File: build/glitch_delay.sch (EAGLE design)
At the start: 55 parts

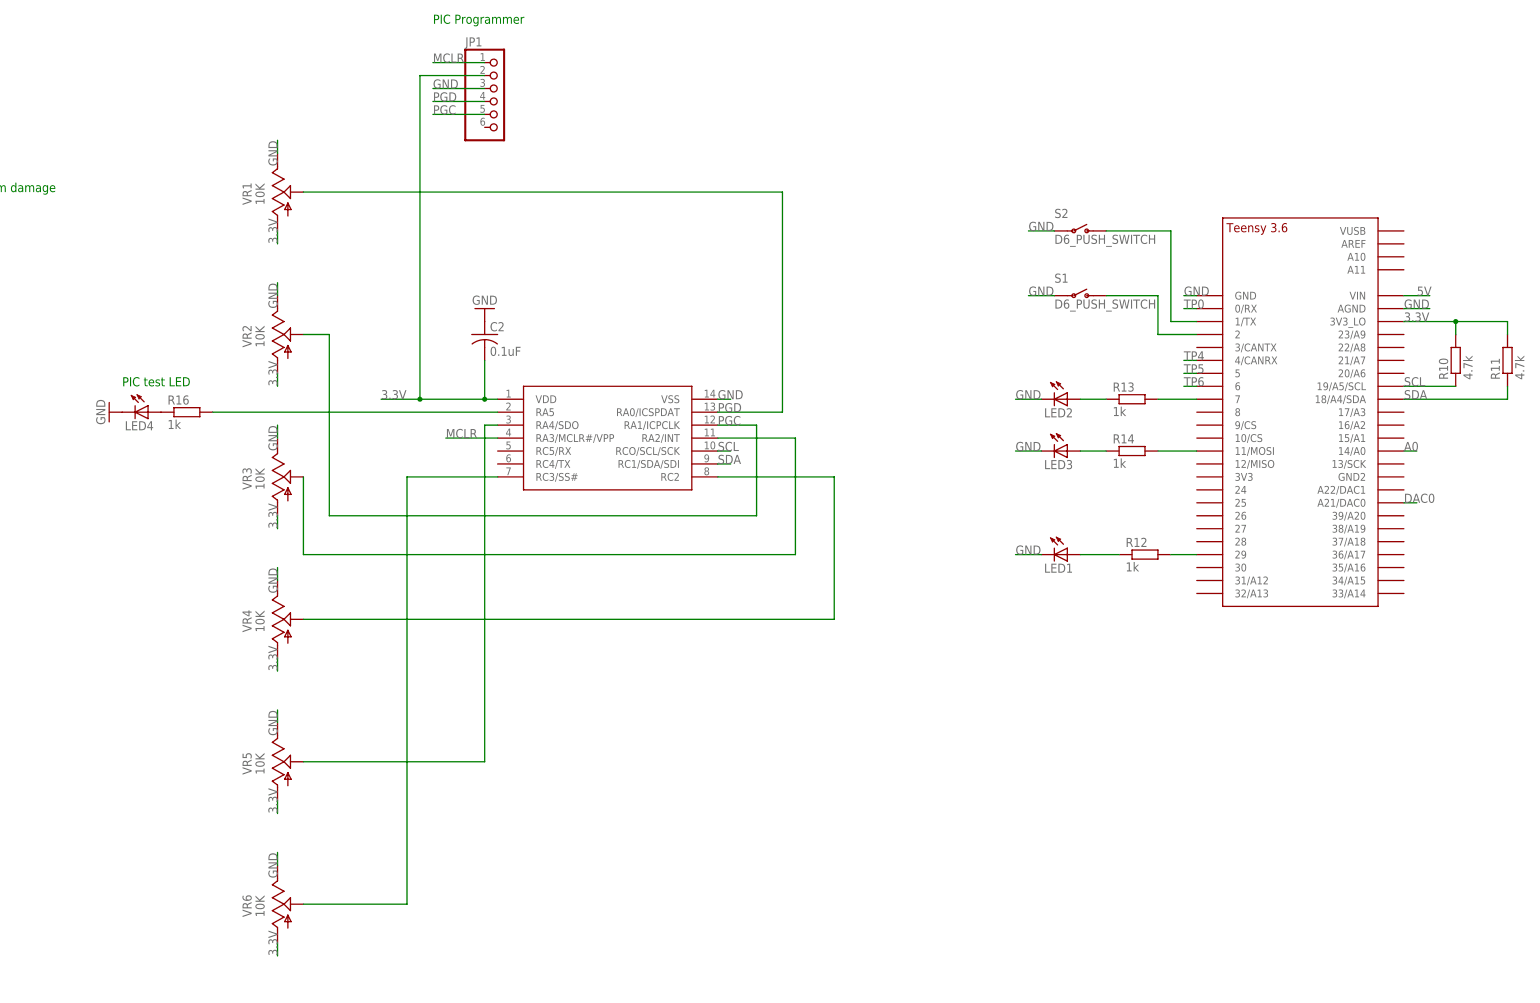
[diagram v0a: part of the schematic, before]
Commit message: Removing PIC from board and using ADC1.
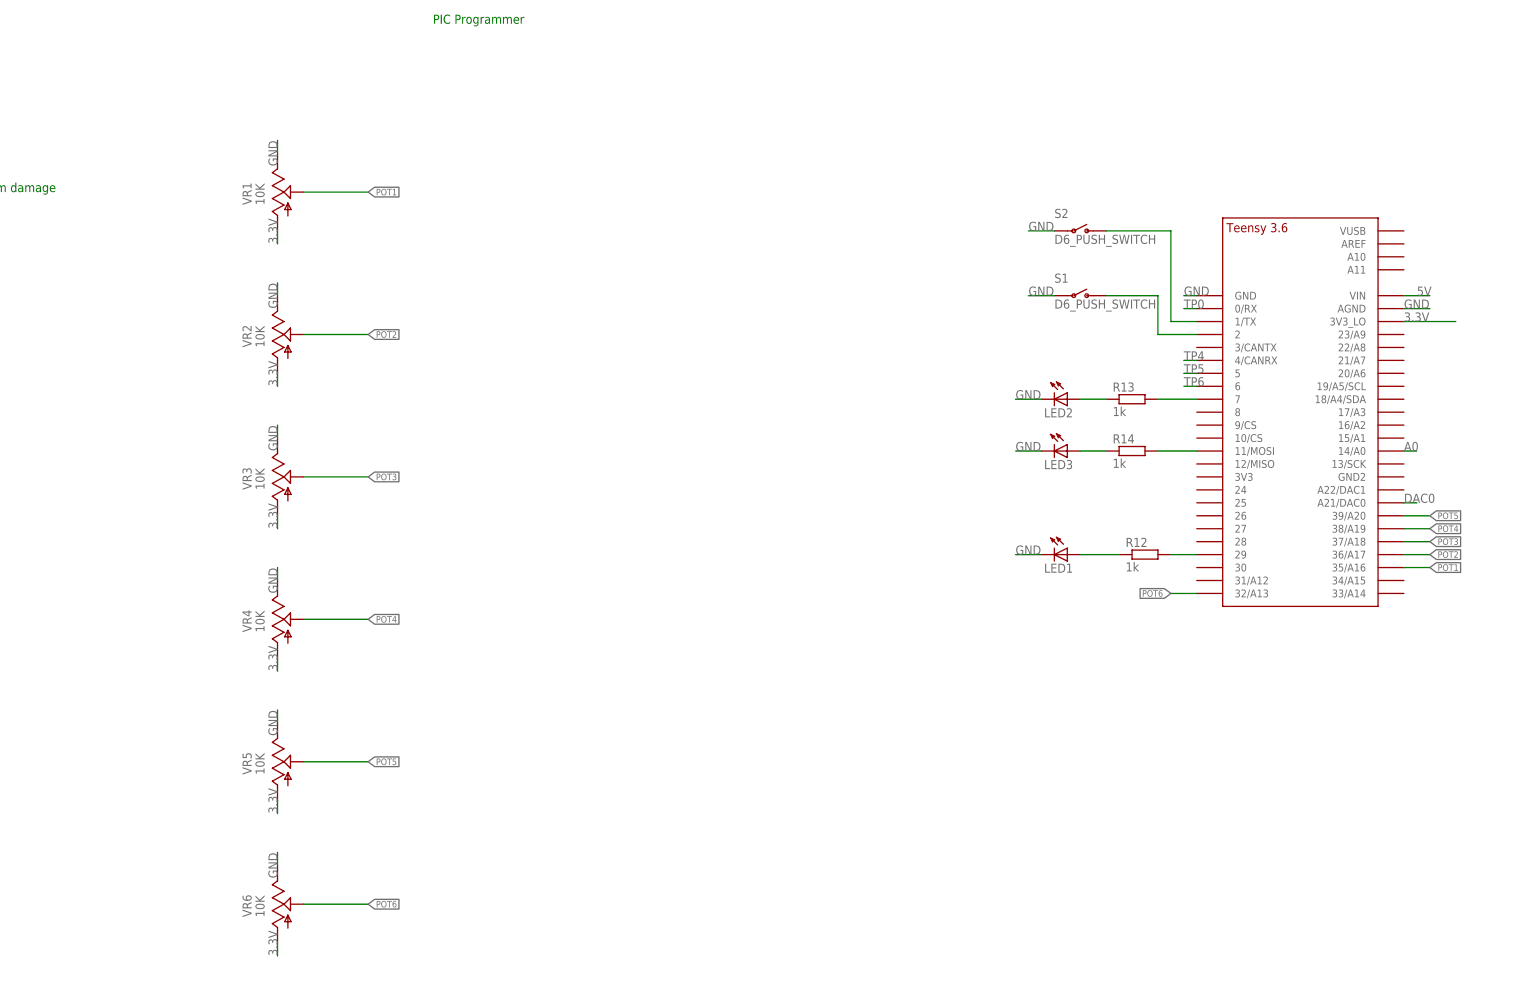
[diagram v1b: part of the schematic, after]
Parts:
- removed C2: 0.1uF, adafruit:C-US025-030X050
- removed JP1: (no value), adafruit:PINHD-1X6
- removed LED4: (no value), adafruit:LED3MM
- removed PIC: PIC16F1825DIL14, jasons_stuff:PIC16F1825DIL14
- removed R10, R11: 4.7k, MusicThingModular:RESISTOR7MM
- removed R16: 1k, MusicThingModular:RESISTOR7MM
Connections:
- removed net MCLR: JP1.1, PIC.RA3/MCLR#/VPP
- removed net N$1: LED4.A, R16.1
- removed net N$10: PIC.RA2/INT, VR3.S
- removed net N$11: PIC.RC2, VR4.S
- removed net N$12: PIC.RA4/SDO, VR5.S
- removed net N$15: PIC.RC3/SS#, VR6.S
- removed net N$5: PIC.RA5, R16.2
- removed net PGC: JP1.5, PIC.RA1/ICPCLK, VR2.S
- removed net PGD: JP1.4, PIC.RA0/ICSPDAT, VR1.S
- new net POT1: U$1.35/A16, VR1.S
- new net POT2: U$1.36/A17, VR2.S
- new net POT3: U$1.37/A18, VR3.S
- new net POT4: U$1.38/A19, VR4.S
- new net POT5: U$1.39/A20, VR5.S
- new net POT6: U$1.32/A13, VR6.S
- net 3.3V: no longer C2.2, JP1.2, PIC.VDD, R10.2, R11.2
- net GND: no longer C2.1, JP1.3, LED4.C, PIC.VSS
- net SCL: no longer PIC.RCO/SCL/SCK, R10.1, U$1.19/A5/SCL
- net SDA: no longer PIC.RC1/SDA/SDI, R11.1, U$1.18/A4/SDA
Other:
- note removed: "PIC test LED"

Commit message: Minor schematic tidying.
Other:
- note removed: "PIC Programmer"
- moved on the sheet: A_IN, A_OUT, C1, C10, C3, C4, C5, C6, C7, C8, C9, D1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
